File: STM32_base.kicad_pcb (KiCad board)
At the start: 2 copper layers, 127 x 50.8 mm, 43 parts, among them J1 TC2030-NL, J2 Conn_01x04_Pin, J3 ST, J4 Conn_01x04_Pin, J5 USB_C_Receptacle_USB2.0_14P, J6 ST, K1 SANYOU_SRD_Form_C, Q1 BC817, SW1 SW_Push, U1 STM32F103C8Tx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

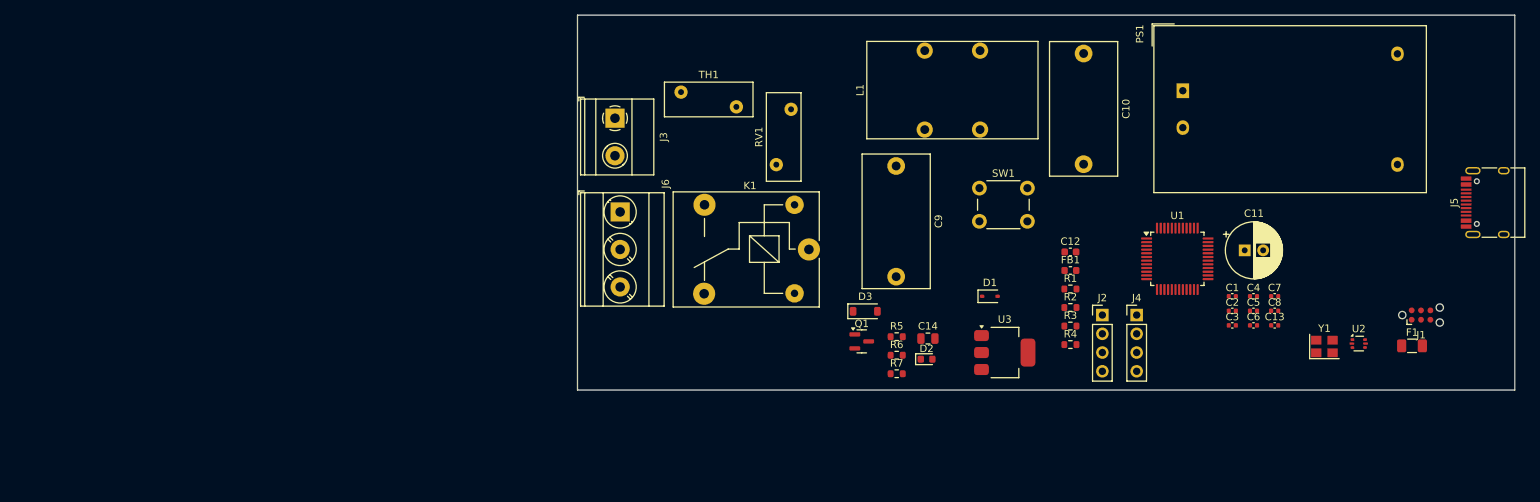
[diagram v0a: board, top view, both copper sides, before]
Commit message: PCB Components placed
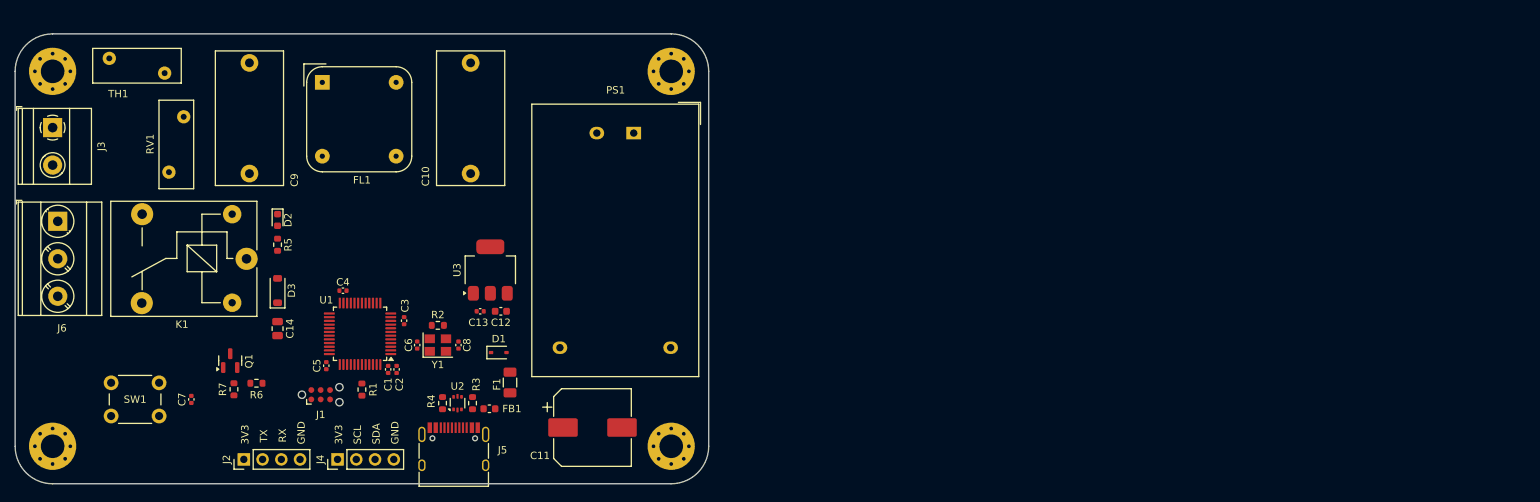
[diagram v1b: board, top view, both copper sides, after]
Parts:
- removed L1: 1mH, Inductor_THT:L_CommonMode_Wuerth_WE-CMB-M
- added FL1: Choke_Schaffner_RN102-2-02-1M1, Inductor_THT:Choke_Schaffner_RN102-04-14.0x14.0mm, F.Cu at (117.8, 85.3)
- added H1: MountingHole_Pad, MountingHole:MountingHole_3.2mm_M3_Pad_Via, F.Cu at (81.3, 134.6)
- added H2: MountingHole_Pad, MountingHole:MountingHole_3.2mm_M3_Pad_Via, F.Cu at (165.1, 83.8)
- added H3: MountingHole_Pad, MountingHole:MountingHole_3.2mm_M3_Pad_Via, F.Cu at (165.1, 134.6)
- added H4: MountingHole_Pad, MountingHole:MountingHole_3.2mm_M3_Pad_Via, F.Cu at (81.3, 83.8)
- C11: footprint Capacitor_THT:CP_Radial_D7.5mm_P2.50mm -> Capacitor_SMD:CP_Elec_10x10
- moved J1 149.5 mm to (117.6, 127.6)
- moved C7 147.5 mm to (100.1, 128.3), turned to 90 degrees
- moved J5 145.4 mm to (135.6, 136.1), turned to 0 degrees
- moved C5 125.9 mm to (118.4, 123.7), turned to -90 degrees
- moved C4 123.4 mm to (120.6, 113.5)
- moved U2 122.4 mm to (136.1, 128.8), turned to 90 degrees
- moved F1 122.3 mm to (143.3, 126.0), turned to 90 degrees
- moved SW1 120.6 mm to (89.2, 126.0)
- moved Y1 120.1 mm to (133.5, 120.9)
- moved J2 118.0 mm to (107.2, 136.4), turned to 90 degrees
- moved C1 114.8 mm to (126.7, 124.2), turned to -90 degrees
- moved C2 113.5 mm to (127.9, 124.2), turned to -90 degrees
- moved C6 113.3 mm to (130.7, 120.9), turned to 90 degrees
- moved C3 112.2 mm to (128.9, 117.6), turned to 90 degrees
- moved U1 111.2 mm to (122.9, 119.4), turned to 180 degrees
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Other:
- board size 127 x 50.8 mm -> 94 x 61 mm
- board text added: "3V3"
- board text added: "GND"
- board text added: "RX"
- board text added: "SCL"
- board text added: "SDA"
- board text added: "TX"

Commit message: pcb finished, gerber added
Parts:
- SW1: value SW_Push -> RST_BTN
- moved D2 5.46 mm to (113.3, 109.2), turned to 90 degrees
- moved R5 3.81 mm to (115.1, 109.2)
- moved D1 2.78 mm to (144.0, 120.3), turned to -90 degrees
- moved FB1 2.77 mm to (140.8, 126.8)
- moved U2 2.05 mm to (135.9, 126.7)
- moved R3 2.05 mm to (137.9, 126.7)
- moved R4 2.05 mm to (133.9, 126.7)
- moved C14 2.03 mm to (113.8, 118.7)
- moved D3 2.03 mm to (113.8, 113.5)
- moved J5 1.55 mm to (135.9, 134.6)
- moved J3 1.23 mm to (82.5, 91.3)
- moved F1 0.97 mm to (144.0, 125.3)
- moved C7 0.91 mm to (100.1, 129.2)
- moved J6 0.82 mm to (82.8, 104.1)
- moved C6 0.76 mm to (130.7, 121.7)
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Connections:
- J2 pad 2: USART_TX -> USART1_TX
- J2 pad 3: USART_RX -> USART1_RX
- R6 pad 1: unconnected-(R6-Pad1) -> Relay_Ctrl
- U1 pad 31: unconnected-(U1-PA10-Pad31) -> Relay_Ctrl
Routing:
- net +3V3: track 0.00 -> 110.1 mm, vias 0 -> 4
- net +5V: track 0.00 -> 86.3 mm, vias 0 -> 2
- net NRST: track 0.00 -> 50.5 mm, vias 0 -> 4
- net Net-(C9-Pad1): track 0.00 -> 40.8 mm
- net /LINE-OUT: track 0.00 -> 38.9 mm
- net /NEUT-OUT: track 0.00 -> 30.4 mm
- net Net-(D2-K): track 0.00 -> 30.1 mm, vias 0 -> 2
- net GND: track 0.00 -> 25.2 mm, vias 0 -> 31
- net Net-(J6-Pin_2): track 0.00 -> 24.8 mm
- net USART1_TX: track 0.00 -> 22.3 mm, vias 0 -> 2
- net USB_D+: track 0.00 -> 20.8 mm, vias 0 -> 2
- net USART1_RX: track 0.00 -> 20.2 mm, vias 0 -> 2
- net USB_D-: track 0.00 -> 19.1 mm, vias 0 -> 2
- net I2C1_SCL: track 0.00 -> 13.6 mm
- net Relay_Ctrl: track 0.00 -> 13.3 mm, vias 0 -> 2
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- added copper zone on B.Cu, net GND
- added copper zone on F.Cu, net GND
- added copper zone on B.Cu, net LINE
- added copper zone on F.Cu, net LINE
- added copper zone on B.Cu, net NEUT
- added copper zone on F.Cu, net NEUT
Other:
- outline, holes or cut-outs redrawn
- board text added: "RST"
